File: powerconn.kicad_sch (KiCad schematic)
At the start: 14 parts, among them CN1 Conn_01x01, CN2 Conn_01x01, CN3 Conn_01x01, K1 G2RL-1A-H, Q1 MMBT3904

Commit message: Cleaning up layout
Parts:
- R25: value Polyfuse -> JK250-080U
- VR1: value Varistor_US -> 07D-418K
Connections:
- net NEUTRAL_OUT renamed NEUTRAL_LOAD
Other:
- note removed: "NEUTRAL_IN is also GND"
- moved on the sheet: C17, CN1, CN2, D4, H1, H2, K1, Q1, R10, R22, R25, VR1

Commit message: All parts on. Set foots for everything. Time to try a layout.
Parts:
- C17: footprint (none) -> Capacitor_SMD:C_0603_1608Metric
- CN1, CN2, CN3, H1, H2, H3: footprint (none) -> Connector_PinHeader_2.54mm:PinHeader_1x01_P2.54mm_Vertical
- D4: footprint Diode_THT:D_DO-41_SOD81_P10.16mm_Horizontal -> Diode_SMD:D_SOD-123F
- K1: footprint Relay_THT:Relay_SPST_Omron_G2RL-1A -> HF relays:HF_Relay_subminature_A_THT_18.4x10.2mm
- R10: footprint (none) -> Resistor_SMD:R_2512_6332Metric
- R22: footprint (none) -> Resistor_SMD:R_0402_1005Metric
- R25: footprint (none) -> Fuse:Fuse_Littelfuse_395Series
- VR1: footprint (none) -> Varistor:RV_Disc_D9mm_W6.1mm_P5mm
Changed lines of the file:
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@@
 	(text "HOT"
 		(exclude_from_sim no)
-		(at 220.98 81.28 0)
+		(at 223.52 85.09 0)
 		(effects
 			(font
@@
 	(text "HOT"
 		(exclude_from_sim no)
-		(at 80.772 81.788 0)
+		(at 80.518 85.344 0)
 		(effects
 			(font
@@
 			)
 		)
-		(property "Footprint" "Relay_THT:Relay_SPST_Omron_G2RL-1A"
+		(property "Footprint" "HF relays:HF_Relay_subminature_A_THT_18.4x10.2mm"
 			(at 160.02 88.9 0)
 			(effects
@@
 			)
 		)
-		(property "Footprint" "Diode_THT:D_DO-41_SOD81_P10.16mm_Horizontal"
+		(property "Footprint" "Diode_SMD:D_SOD-123F"
 			(at 161.29 50.165 0)
 			(effects
@@
 			)
 		)
-		(property "Footprint" ""
+		(property "Footprint" "Resistor_SMD:R_0402_1005Metric"
 			(at 117.094 47.244 90)
 			(effects
@@
 			)
 		)
-		(property "Footprint" ""
+		(property "Footprint" "Capacitor_SMD:C_0603_1608Metric"
 			(at 165.1 39.6748 0)
 			(effects
@@
 			)
 		)
-		(property "Footprint" ""
+		(property "Footprint" "Resistor_SMD:R_2512_6332Metric"
 			(at 162.814 128.524 90)
 			(effects
@@
 			)
 		)
-		(property "Footprint" ""
+		(property "Footprint" "Connector_PinHeader_2.54mm:PinHeader_1x01_P2.54mm_Vertical"
 			(at 91.44 129.54 0)
 			(effects
@@
 			)
 		)
-		(property "Footprint" ""
+		(property "Footprint" "Varistor:RV_Disc_D9mm_W6.1mm_P5mm"
 			(at 122.682 119.38 90)
 			(effects
@@
 			)
 		)
-		(property "Footprint" ""
+		(property "Footprint" "Connector_PinHeader_2.54mm:PinHeader_1x01_P2.54mm_Vertical"
 			(at 91.44 85.09 0)
 			(effects
@@
 			)
 		)
-		(property "Footprint" ""
+		(property "Footprint" "Connector_PinHeader_2.54mm:PinHeader_1x01_P2.54mm_Vertical"
 			(at 203.2 129.54 0)
 			(effects
@@
 			)
 		)
-		(property "Footprint" ""
+		(property "Footprint" "Connector_PinHeader_2.54mm:PinHeader_1x01_P2.54mm_Vertical"
 			(at 203.2 85.09 0)
 			(effects
@@
 			)
 		)
-		(property "Footprint" ""
+		(property "Footprint" "Connector_PinHeader_2.54mm:PinHeader_1x01_P2.54mm_Vertical"
 			(at 91.44 160.02 0)
 			(effects
@@
 			)
 		)
-		(property "Footprint" ""
+		(property "Footprint" "Fuse:Fuse_Littelfuse_395Series"
 			(at 125.73 102.87 0)
 			(effects
@@
 			)
 		)
-		(property "Footprint" ""
+		(property "Footprint" "Connector_PinHeader_2.54mm:PinHeader_1x01_P2.54mm_Vertical"
 			(at 203.2 160.02 0)
 			(effects

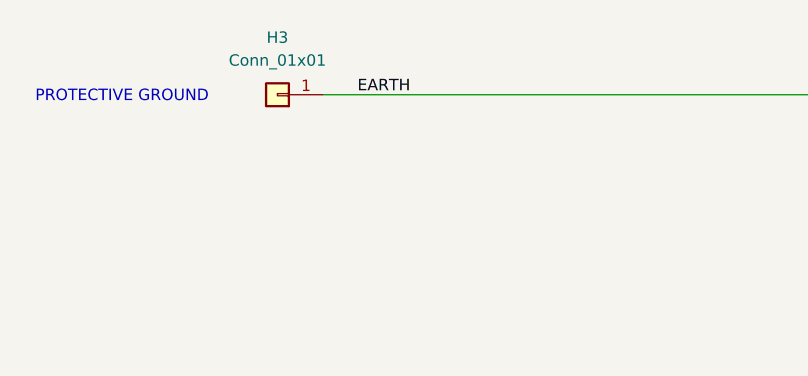
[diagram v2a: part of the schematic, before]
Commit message: Made a first board layout.
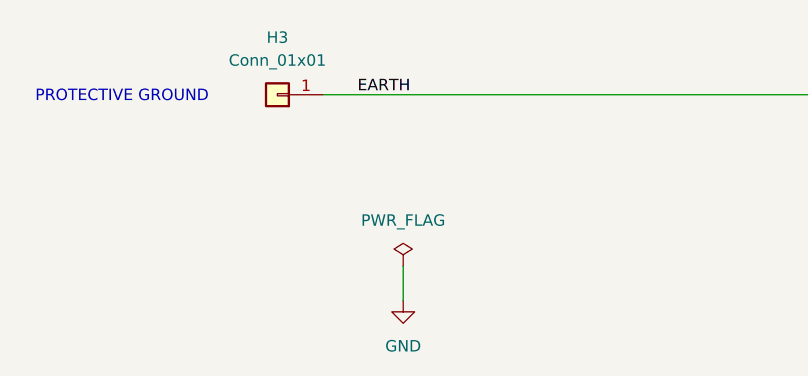
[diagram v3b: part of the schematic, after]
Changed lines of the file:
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@@
+	(wire
+		(pts
+			(xy 105.41 179.07) (xy 105.41 182.88)
+		)
+		(stroke
+			(width 0)
+			(type default)
+		)
+	)
 	(wire
 		(pts
@@
 	)
 	(symbol
+		(lib_id "power:GND")
+		(at 105.41 182.88 0)
+		(unit 1)
+		(exclude_from_sim no)
+		(in_bom yes)
+		(on_board yes)
+		(dnp no)
+		(fields_autoplaced yes)
+		(property "Reference" "#PWR017"
+			(at 105.41 189.23 0)
+			(effects
+				(font
+					(size 1.27 1.27)
+				)
+				(hide yes)
+			)
+		)
+		(property "Value" "GND"
+			(at 105.41 187.96 0)
+			(effects
+				(font
+					(size 1.27 1.27)
+				)
+			)
+		)
+		(property "Footprint" ""
+			(at 105.41 182.88 0)
+			(effects
+				(font
+					(size 1.27 1.27)
+				)
+				(hide yes)
+			)
+		)
+		(property "Datasheet" ""
+			(at 105.41 182.88 0)
+			(effects
+				(font
+					(size 1.27 1.27)
+				)
+				(hide yes)
+			)
+		)
+		(property "Description" "Power symbol creates a global label with name \"GND\" , ground"
+			(at 105.41 182.88 0)
+			(effects
+				(font
+					(size 1.27 1.27)
+				)
+				(hide yes)
+			)
+		)
+		(pin "1"
+		)
+		(instances
+			(project "Meross smart outlet reverse"
+				(path "/0b789f5a-74d1-4f81-bd1f-7ac838c6392e/0d0b8180-7ba4-4dc9-99b6-4281183d15f0"
+					(reference "#PWR017")
+					(unit 1)
+				)
+			)
+		)
+	)
+	(symbol
 		(lib_id "Connector_Generic:Conn_01x01")
 		(at 91.44 160.02 180)
@@
 					(unit 1)
 				)
+			)
+		)
+	)
+	(symbol
+		(lib_id "power:PWR_FLAG")
+		(at 105.41 179.07 0)
+		(unit 1)
+		(exclude_from_sim no)
+		(in_bom yes)
+		(on_board yes)
+		(dnp no)
+		(fields_autoplaced yes)
+		(property "Reference" "#FLG02"
+			(at 105.41 177.165 0)
+			(effects
+				(font
+					(size 1.27 1.27)
+				)
+				(hide yes)
+			)
+		)
+		(property "Value" "PWR_FLAG"
+			(at 105.41 173.99 0)
+			(effects
+				(font
+					(size 1.27 1.27)
+				)
+			)
+		)
+		(property "Footprint" ""
+			(at 105.41 179.07 0)
+			(effects
+				(font
+					(size 1.27 1.27)
+				)
+				(hide yes)
+			)
+		)
+		(property "Datasheet" "~"
+			(at 105.41 179.07 0)
+			(effects
+				(font
+					(size 1.27 1.27)
+				)
+				(hide yes)
+			)
+		)
+		(property "Description" "Special symbol for telling ERC where power comes from"
+			(at 105.41 179.07 0)
+			(effects
+				(font
+					(size 1.27 1.27)
+				)
+				(hide yes)
+			)
+		)
+		(pin "1"
+		)
+		(instances
+			(project ""
+				(path "/0b789f5a-74d1-4f81-bd1f-7ac838c6392e/0d0b8180-7ba4-4dc9-99b6-4281183d15f0"
+					(reference "#FLG02")
+					(unit 1)
+				)

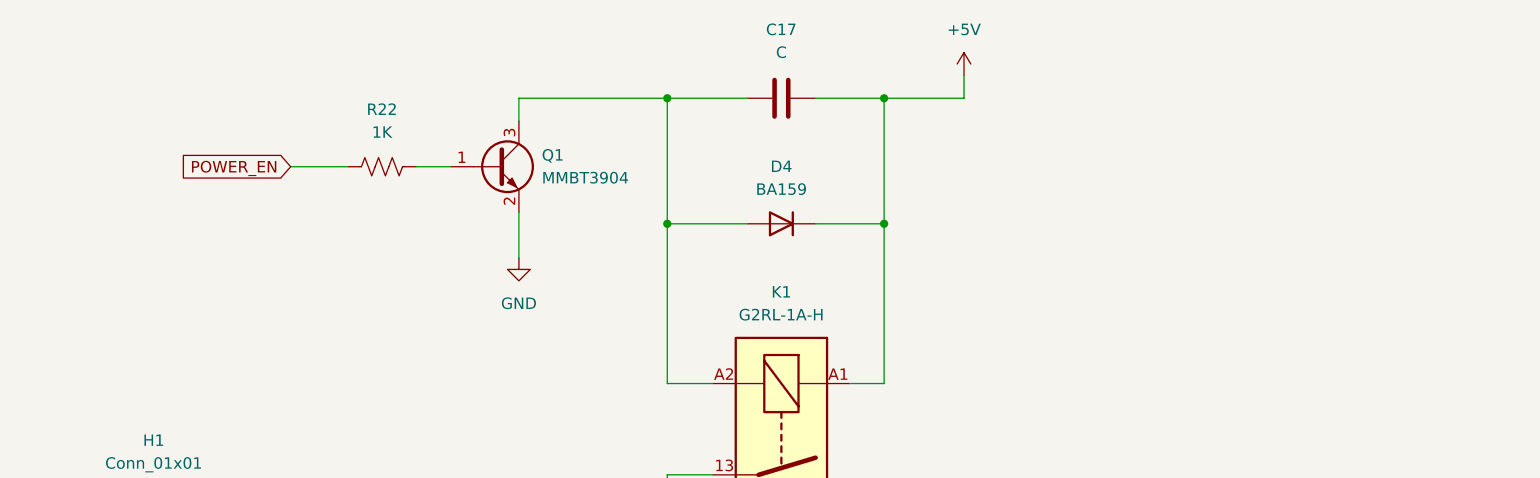
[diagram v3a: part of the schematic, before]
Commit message: Have a full board layout which resembles the original in some ways. Made a few schematic fixes to match better.
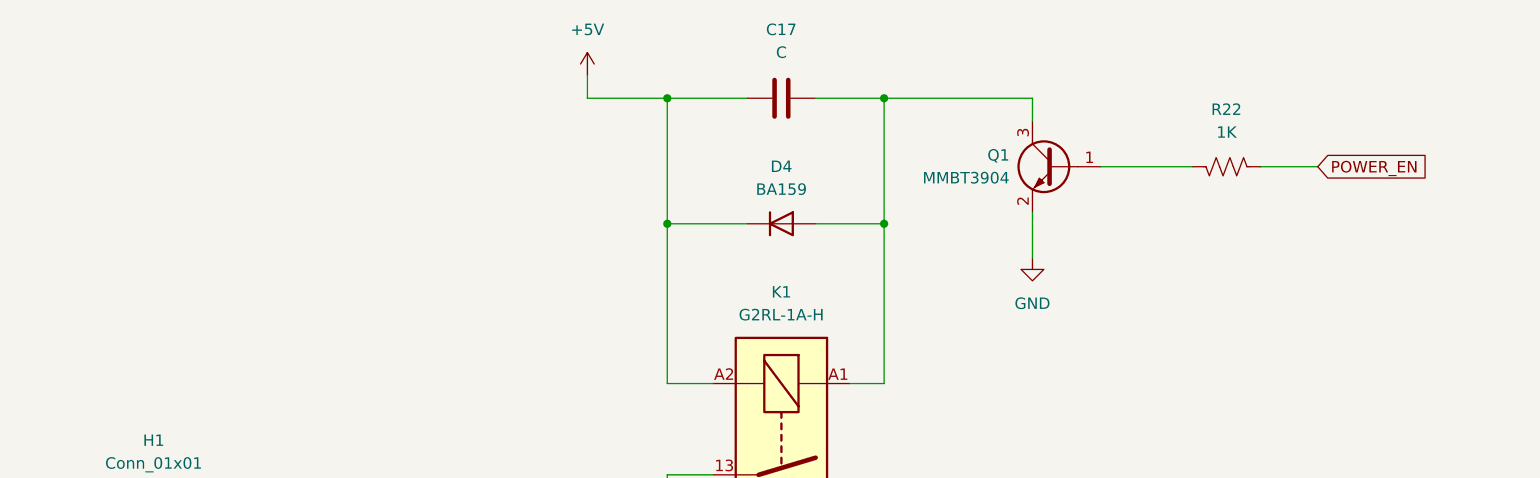
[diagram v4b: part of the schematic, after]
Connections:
- net +5V: now also K1.A2; no longer K1.A1
- net at C17.1, D4.2 (A), Q1.3 (C): now also K1.A1; no longer K1.A2
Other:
- moved on the sheet: C17, D4, Q1, R22

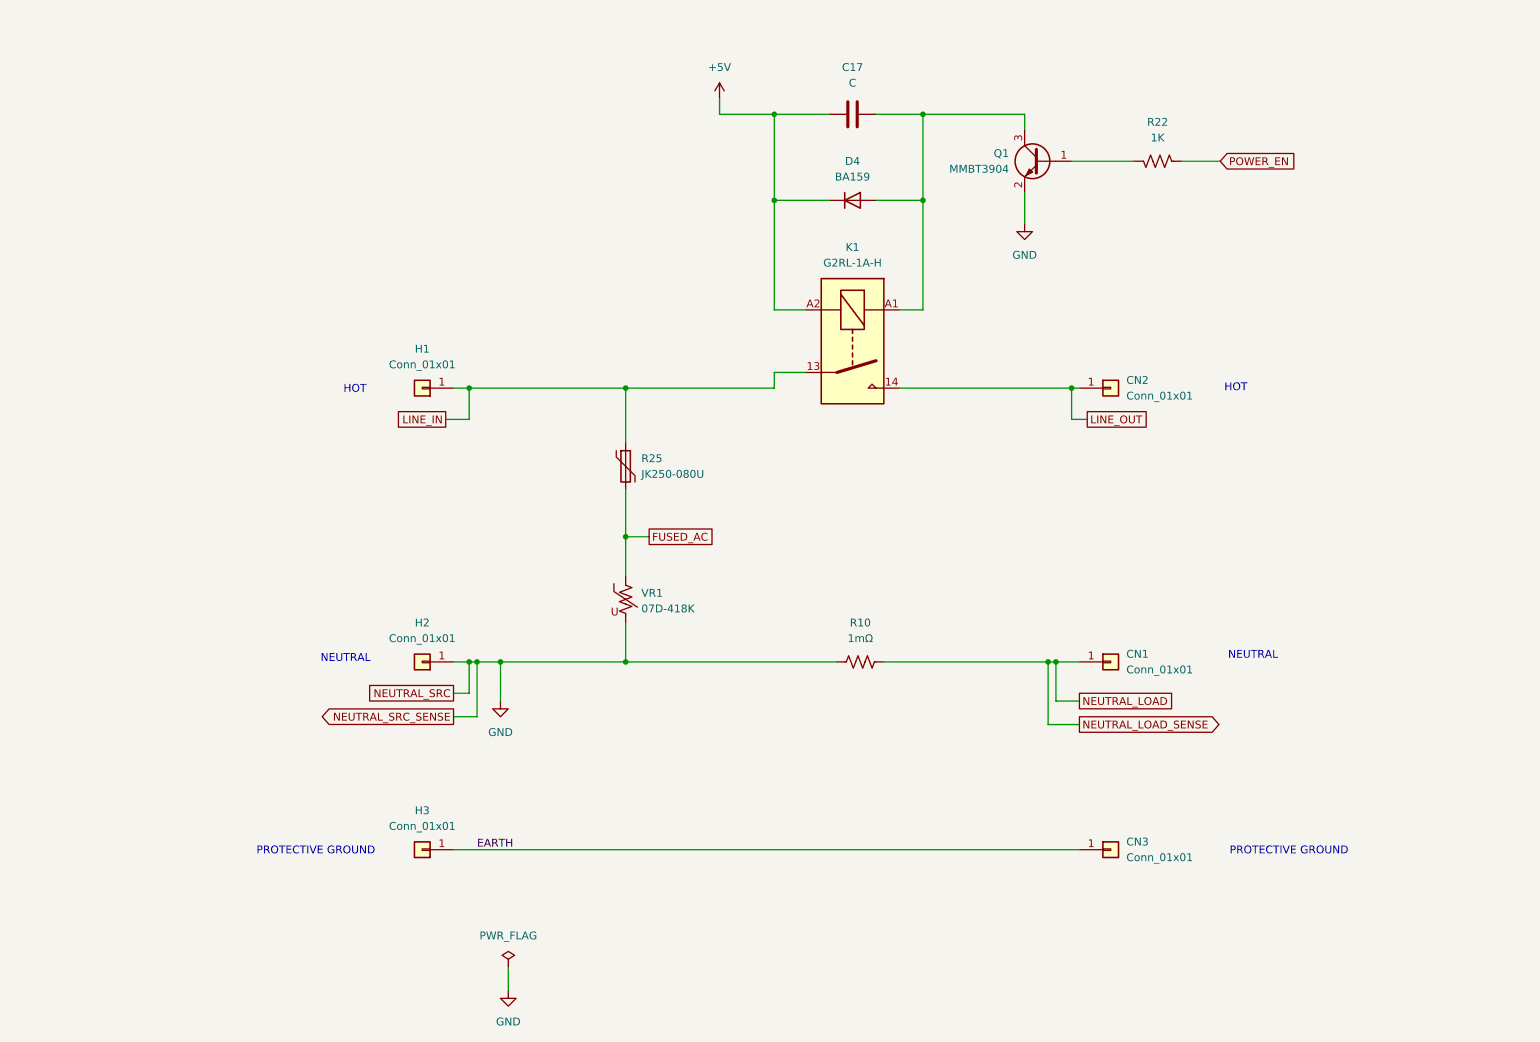
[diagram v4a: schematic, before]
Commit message: Making board layout match better. Added new footprints and symbols.
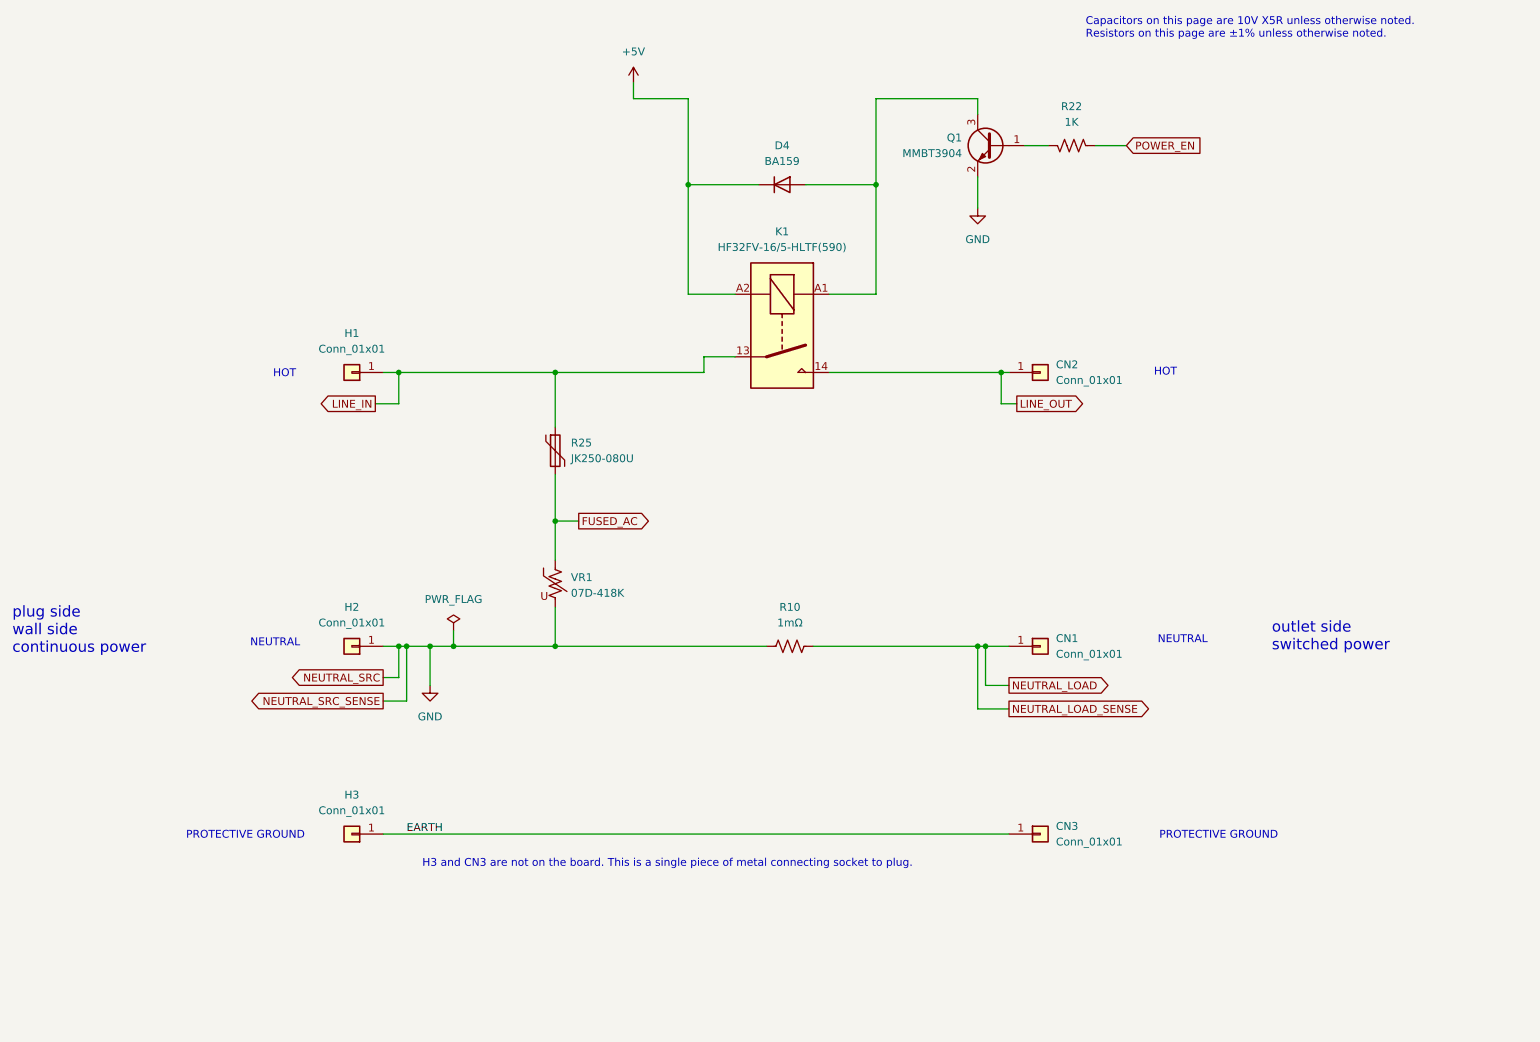
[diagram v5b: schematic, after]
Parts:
- removed C17: C, Capacitor_SMD:C_0603_1608Metric, symbol Device:C
- CN3, H3: now left out of the parts list
- K1: value G2RL-1A-H -> HF32FV-16/5-HLTF(590); symbol Relay:G2RL-1A-H -> Relay:Relay_SPST-NO
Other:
- note added: "Capacitors on this page are 10V X5R unless otherwise noted. Resistors on this page are ±1% unless otherwise noted."
- note added: "H3 and CN3 are not on the board. This is a single piece of metal connecting socket to plug."
- note added: "outlet side switched power"
- note added: "plug side wall side continuous power"
- title: (none) -> power connections and control
- moved on the sheet: CN1, CN2, CN3, D4, H1, H2, H3, K1, Q1, R10, R22, R25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
